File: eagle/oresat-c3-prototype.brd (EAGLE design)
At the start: 99.8 x 94.7 mm, 98 parts, among them J1 J-SAMTEC-TFM-110-X1-XXX-D-RA, J2 U.FL, J3 U.FL, J4 U.FL, J6 J-SAMTEC-TFM-120-X1-XXX-D-RA, J7 FTSH-105-XX-X-DV-K, J8 SD_CARD_SOCKET, Q1 MOSFET-PCH-SOT23-6, Q3 MOSFET-PCH-SOT23-6, Q4 MOSFET-PCH-SOT23-6, Q5 PMV45EN, Q6 PMV45EN, U2 TCAN330, U3 TCAN330, U4 MAX4211CETE, U5 TPS62111RSA, U6 MAX6373KA+21-0078H-L, X1 16MHZ-2.5x2mm

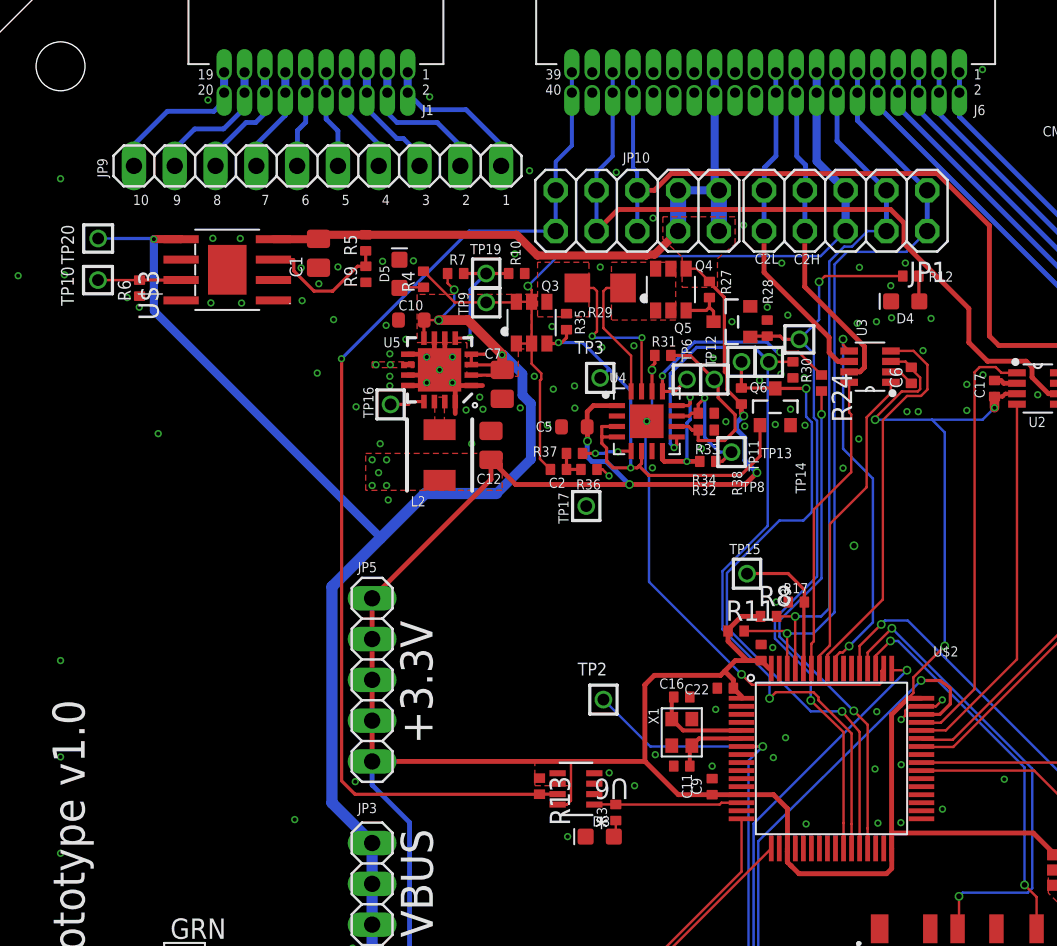
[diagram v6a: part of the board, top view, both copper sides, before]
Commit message: Switched the MAX892 in for the OPD circuit breaker and rerouted the wires
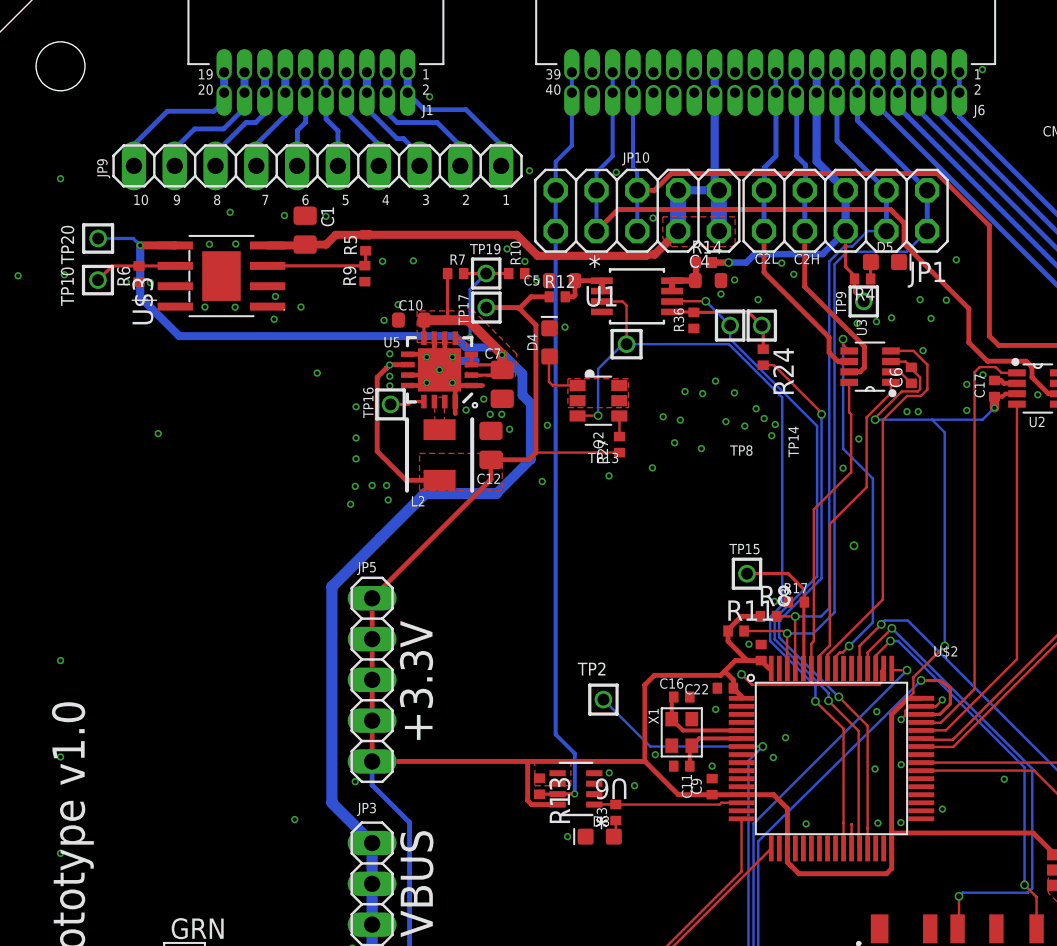
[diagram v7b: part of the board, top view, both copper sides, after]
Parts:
- removed C2, R32, R34, R37: NP, rcl_custom:.0402-B-NOSILK
- removed Q3, Q4: MOSFET-PCH-SOT23-6, Q-MOSFET-PCH-SOT23-6:SOT23-6
- removed Q5, Q6: PMV45EN, Tova:SOT23
- removed R28, R30, R35, R38: 10k, rcl_custom:.0402-B-NOSILK
- removed R29: 100m, rcl:R1206
- removed R31, R33: 0, rcl_custom:.0402-B-NOSILK
- removed TP11, TP12, TP3, TP6: TEST-POINT, Tova:2MM-TEST-POINT
- removed U4: MAX4211CETE, U-Maxim-MAX4211-power-monitor:QFN65P400X400X80-17T210
- added C4: 0.1u, oresat-rcl:.0603-B-NOSILK
- added Q2: MOSFET-PCH-SOT23-6, Q-MOSFET-PCH-SOT23-6:SOT23-6
- added R14: 0, rcl_custom:.0402-B-NOSILK
- added U1: MAX892LEUA+T, Robins_Parts:21-0036K
- R12: value 2.7k -> 0
- R36: value NP -> 23.9k
- U$3: value TI-TPS259621-eFuse -> (none)
- moved D5 30.2 mm to (57.3, 76.8), turned to 0 degrees
- moved R4 27.3 mm to (55.9, 75.8), turned to 180 degrees
- moved TP9 23.5 mm to (56.0, 74.4)
- moved D4 22.3 mm to (36.4, 71.8), turned to 90 degrees
- moved R12 22.0 mm to (36.9, 74.7), turned to 0 degrees
- moved TP17 13.8 mm to (32.5, 74.0)
- moved R36 11.3 mm to (45.4, 73.2), turned to 90 degrees
- moved R27 11.2 mm to (40.8, 65.5), turned to 270 degrees
- moved TP13 10.8 mm to (41.2, 71.7)
- moved C5 9.13 mm to (37.2, 75.7)
- moved R24 3.97 mm to (49.8, 70.9)
- moved TP8 2.37 mm to (47.7, 72.9)
- moved TP14 2.30 mm to (49.7, 72.9)
- moved C1 1.66 mm to (21.2, 78.8), turned to 270 degrees
- moved R6 0.88 mm to (10.9, 76.1)
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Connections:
- removed net CB_CTRL: Q3.3, Q6.1, R35.1, TP3.1, U4.3, U4.4, U4.6
- removed net N$398: Q3.4, R29.2, R35.2, U4.15
- removed net N$575: D4.A, R12.1
- removed net N$590: Q4.3, Q5.3, R27.1
- removed net N$593: Q4.1, Q4.2, Q4.5, Q4.6, R29.1, U4.16
- removed net N$596: R31.1, R32.2, TP12.1, U4.10
- removed net N$597: R33.1, R34.2, TP11.1, U4.11
- removed net N$599: R33.2, U4.12, U4.8
- removed net N$603: C2.1, R36.2, R37.2
- removed net N$604: R37.1, U4.5
- removed net OPD_POUT: R24.1, TP6.1, U4.13
- new net OPD_I_SET: R24.1, R36.2, TP14.1, U1.5
- new net OPD_ON/LED: D4.A, Q2.1, Q2.2, Q2.5, Q2.6
- new net OPD_ON/LED_SWITCH: Q2.4, R27.1
- net 3.3V: now also R12.1, R12.2, U1.1, U1.2; no longer Q4.4, R38.2, U4.1
- net GND: now also C4.2, U1.4; no longer Q5.2, Q6.2, R28.1, R30.1, R32.1, R34.1, U4.7, U4.EPAD
- net ILIM: now also U$3.6; no longer U$3.7
- net OPD_!FAULT: now also U1.6; no longer Q6.3, R38.1
- net OPD_CB_RESET: no longer R30.2, TP14.1, U4.9
- net OPD_ON/!OFF: now also Q2.3, U1.3; no longer Q5.1, R12.2, R28.2
- net OPD_PWR: now also C4.1, R14.1, R14.2, U1.7, U1.8; no longer C2.2, Q3.1, Q3.2, Q3.5, Q3.6
- net PA15: no longer R31.2, U4.14
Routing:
- net OPD_CB_RESET: track 51.1 -> 1.53 mm, vias 2 -> 0
- net CB_CTRL: track 30.8 -> 0.00 mm, vias 2 -> 0
- net OPD_PWR: track 52.4 -> 27.9 mm
- net PA15: track 34.0 -> 9.96 mm, vias 2 -> 1
- net !SD: track 67.0 -> 48.0 mm
- net OPD_POUT: track 14.5 -> 0.00 mm, vias 2 -> 0
- net N$596: track 11.7 -> 0.00 mm
- net N$398: track 10.7 -> 0.00 mm, vias 2 -> 0
- net N$599: track 8.27 -> 0.00 mm, vias 2 -> 0
- net N$593: track 8.26 -> 0.00 mm
- net N$597: track 8.25 -> 0.00 mm, vias 1 -> 0
- net OPD_I_SET: track 0.00 -> 7.48 mm
- net OPD_ON/!OFF: track 47.7 -> 52.0 mm
- net OPD_POUT_IN: track 31.9 -> 35.4 mm
- net OPD_ON/LED: track 0.00 -> 3.46 mm
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- added copper zone on layer 1, net OPD_ON/LED
- removed copper zone on layer 1, net N$398
- removed copper zone on layer 1, net N$593

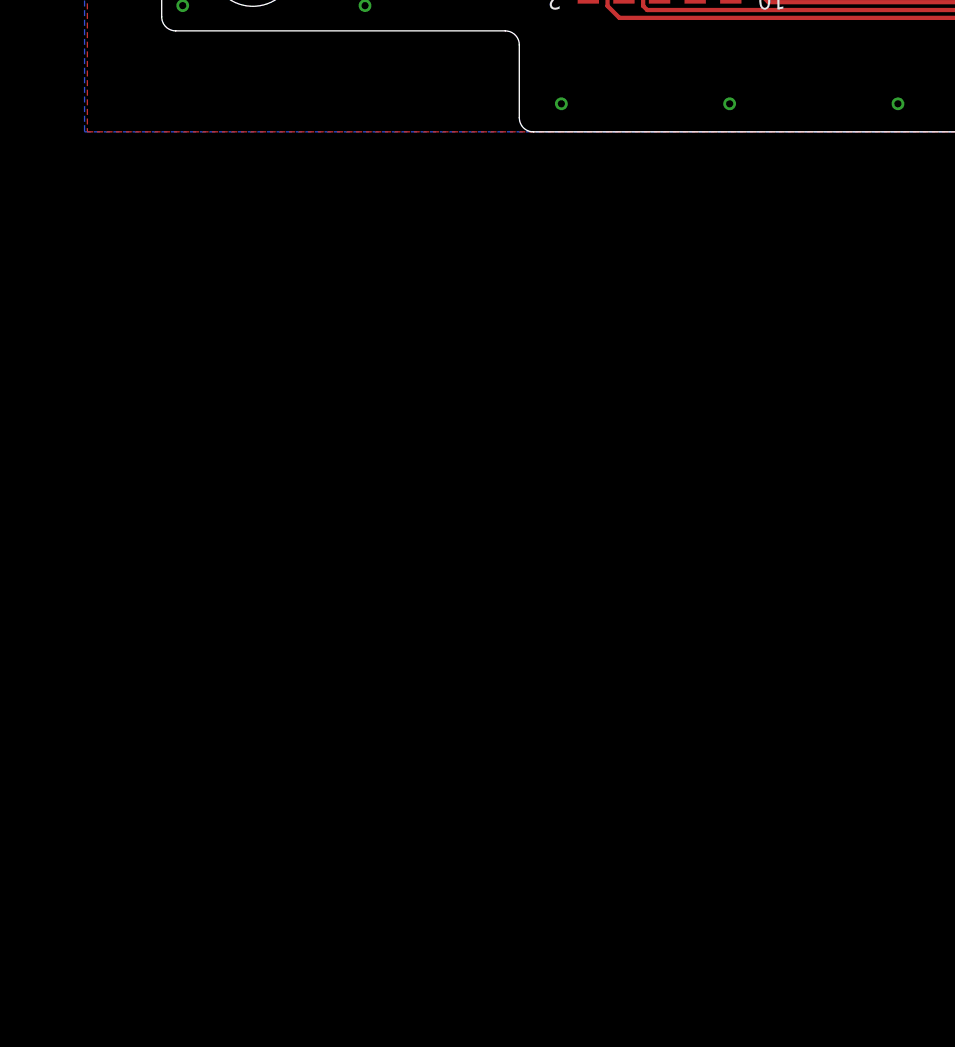
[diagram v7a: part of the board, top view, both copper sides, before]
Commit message: Added 2 radio headers and associated test points to sheet 1. Components need to be placed and nets named appropriately
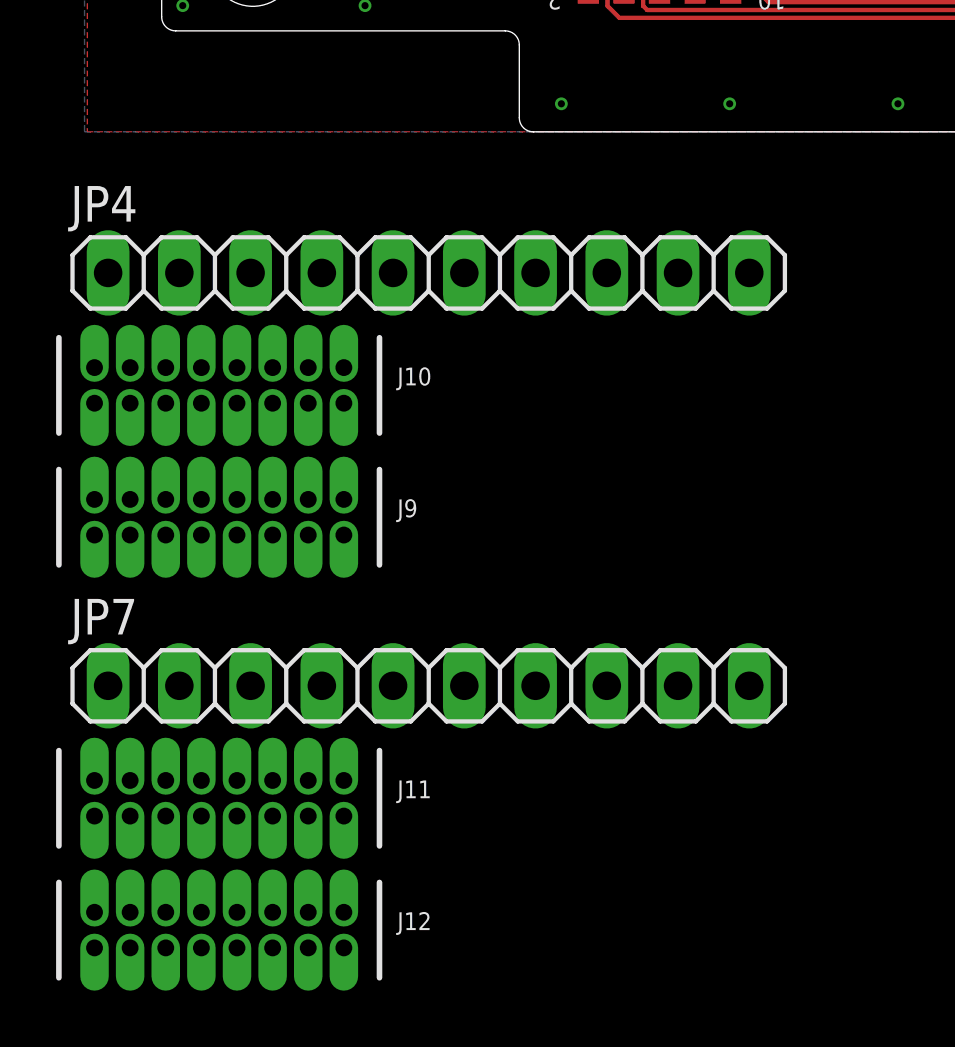
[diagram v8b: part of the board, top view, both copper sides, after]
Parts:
- added J10, J11, J12, J9: 2X8X1.27, 2x8x1.27:2X8X1.27
- added JP4, JP7: (no value), pinhead:1X10
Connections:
- new net CLK: J10.7, J12.7, JP4.8, JP7.8
- new net IRQ: J10.13, J12.13, JP4.5, JP7.5
- new net MISO: J10.9, J12.9, JP4.7, JP7.7
- new net MOSI: J10.11, J12.11, JP4.6, JP7.6
- new net SEI: J10.5, J12.5, JP4.9, JP7.9
- new net SYSCLK: J10.3, J12.3, JP4.10, JP7.10
- net 3.3V: now also J11.13, J11.3, J9.13, J9.3, JP4.1, JP4.2, JP7.1, JP7.2
- net GND: now also J10.1, J10.10, J10.12, J10.14, J10.15, J10.16, J10.2, J10.4, J10.6, J10.8, J11.1, J11.10, J11.12, J11.14, J11.15, J11.16, J11.2, J11.4, J11.6, J11.8, J12.1, J12.10, J12.12, J12.14, J12.15, J12.16, J12.2, J12.4, J12.6, J12.8, J9.1, J9.10, J9.12, J9.14, J9.15, J9.16, J9.2, J9.4, J9.6, J9.8, JP4.3, JP4.4, JP7.3, JP7.4
